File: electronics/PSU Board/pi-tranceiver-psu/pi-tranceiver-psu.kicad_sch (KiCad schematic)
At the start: 37 parts, among them IC1 LTC4368IMS-2#PBF, Q1 DMT6002LPS-13, Q2 DMT6002LPS-13

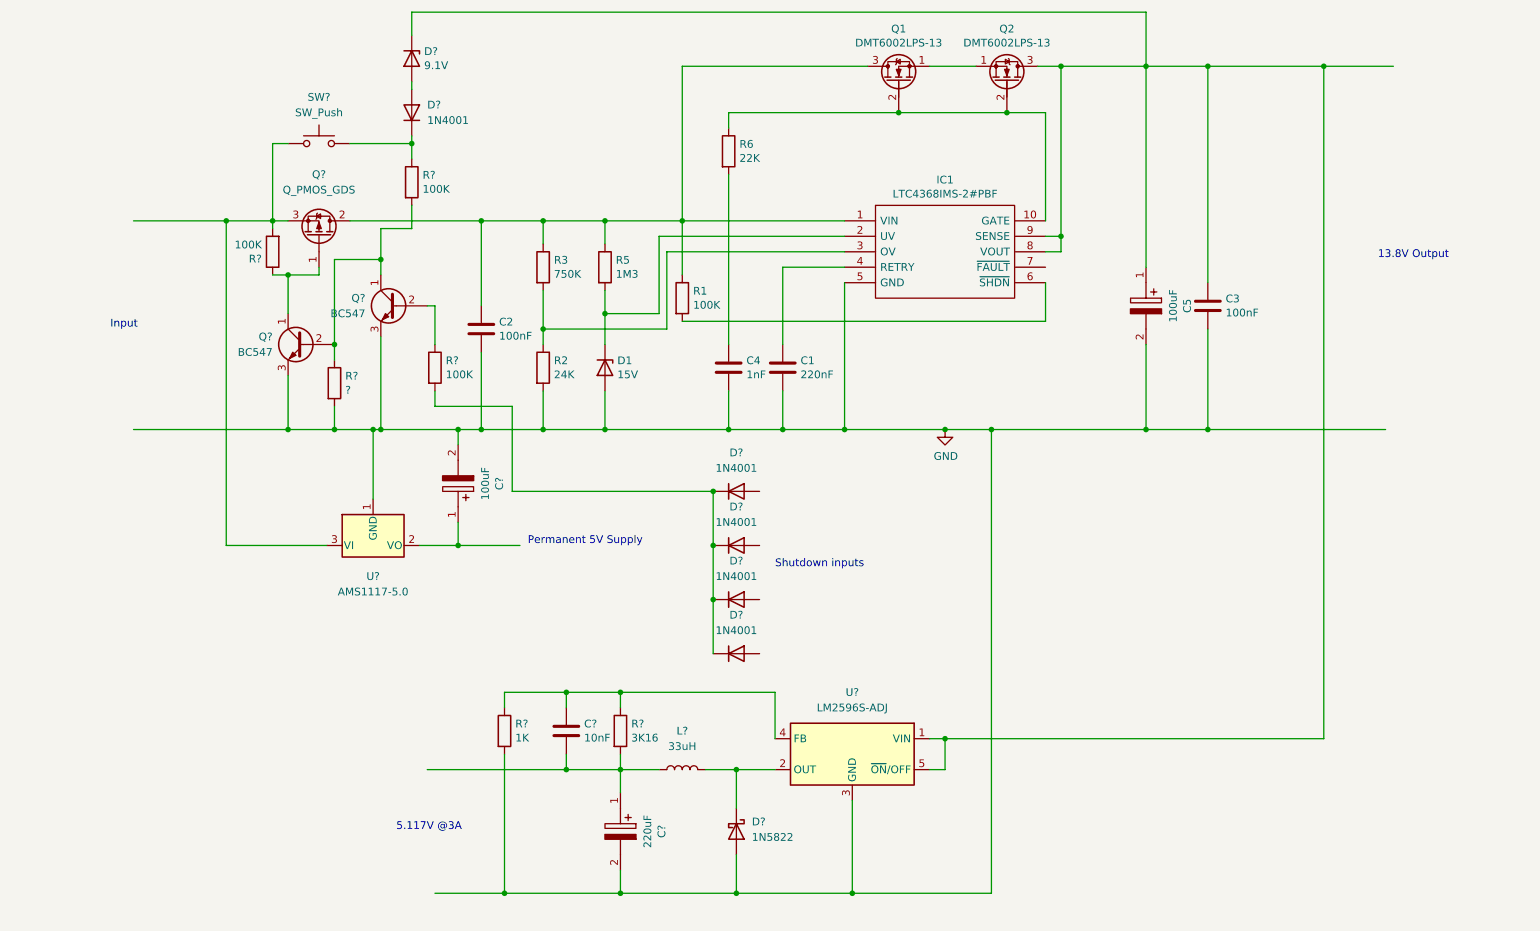
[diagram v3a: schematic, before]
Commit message: Added LM2679 details and project library
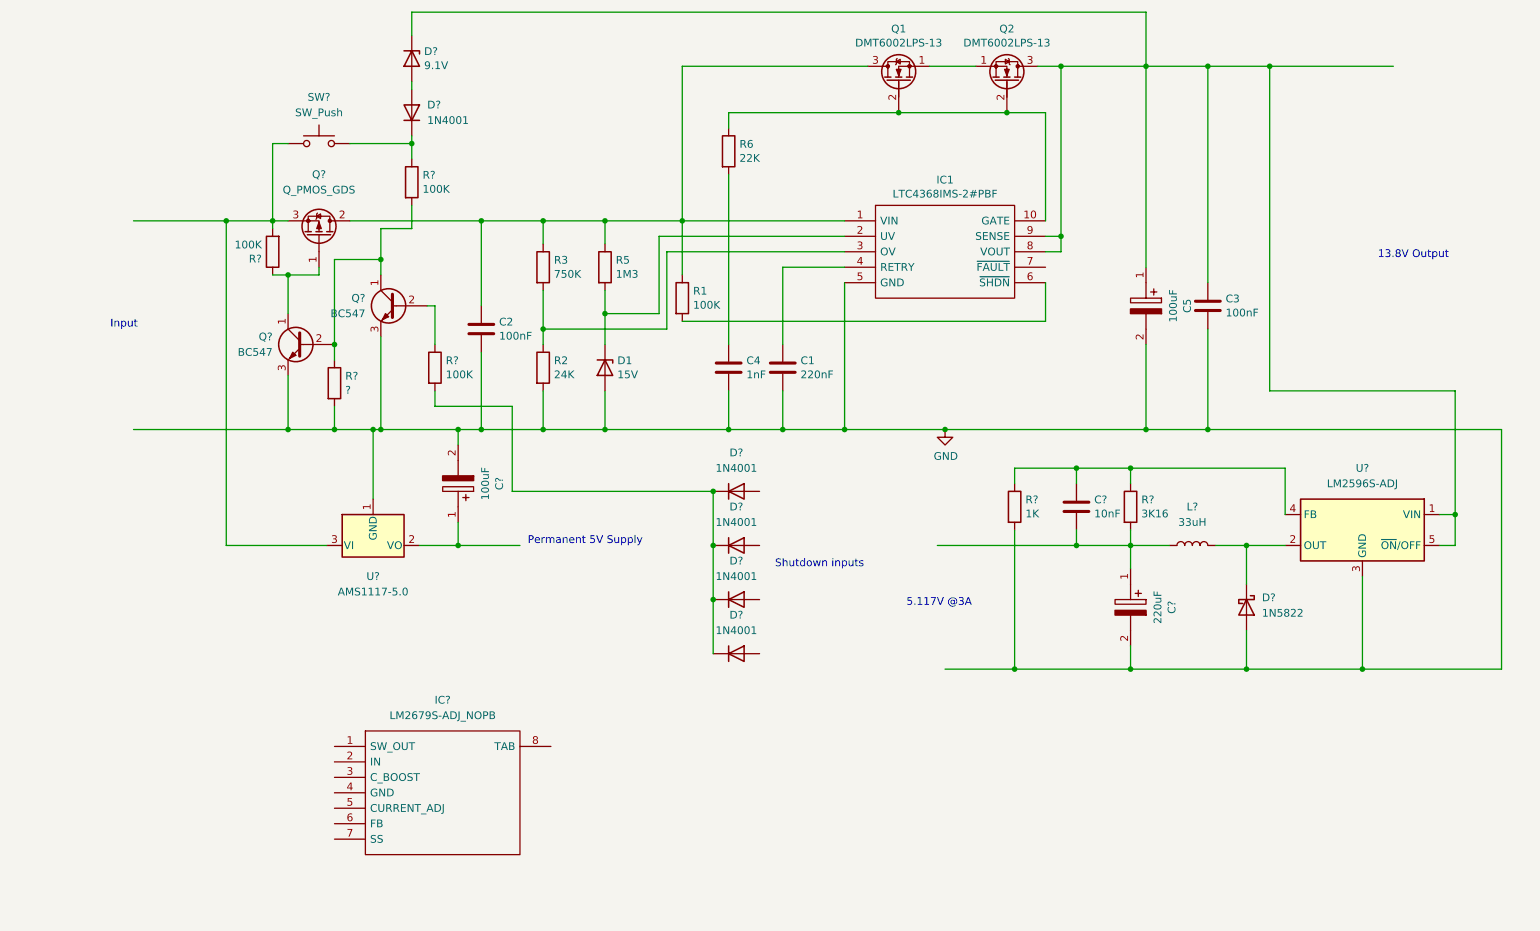
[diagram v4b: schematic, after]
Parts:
- added IC?: LM2679S-ADJ_NOPB, PSU_Board:TO127P1435X464-8N, symbol PSU_Board:LM2679S-ADJ_NOPB
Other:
- moved on the sheet: C?, D?, L?, R?, U?

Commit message: New PSU Design and added connectors
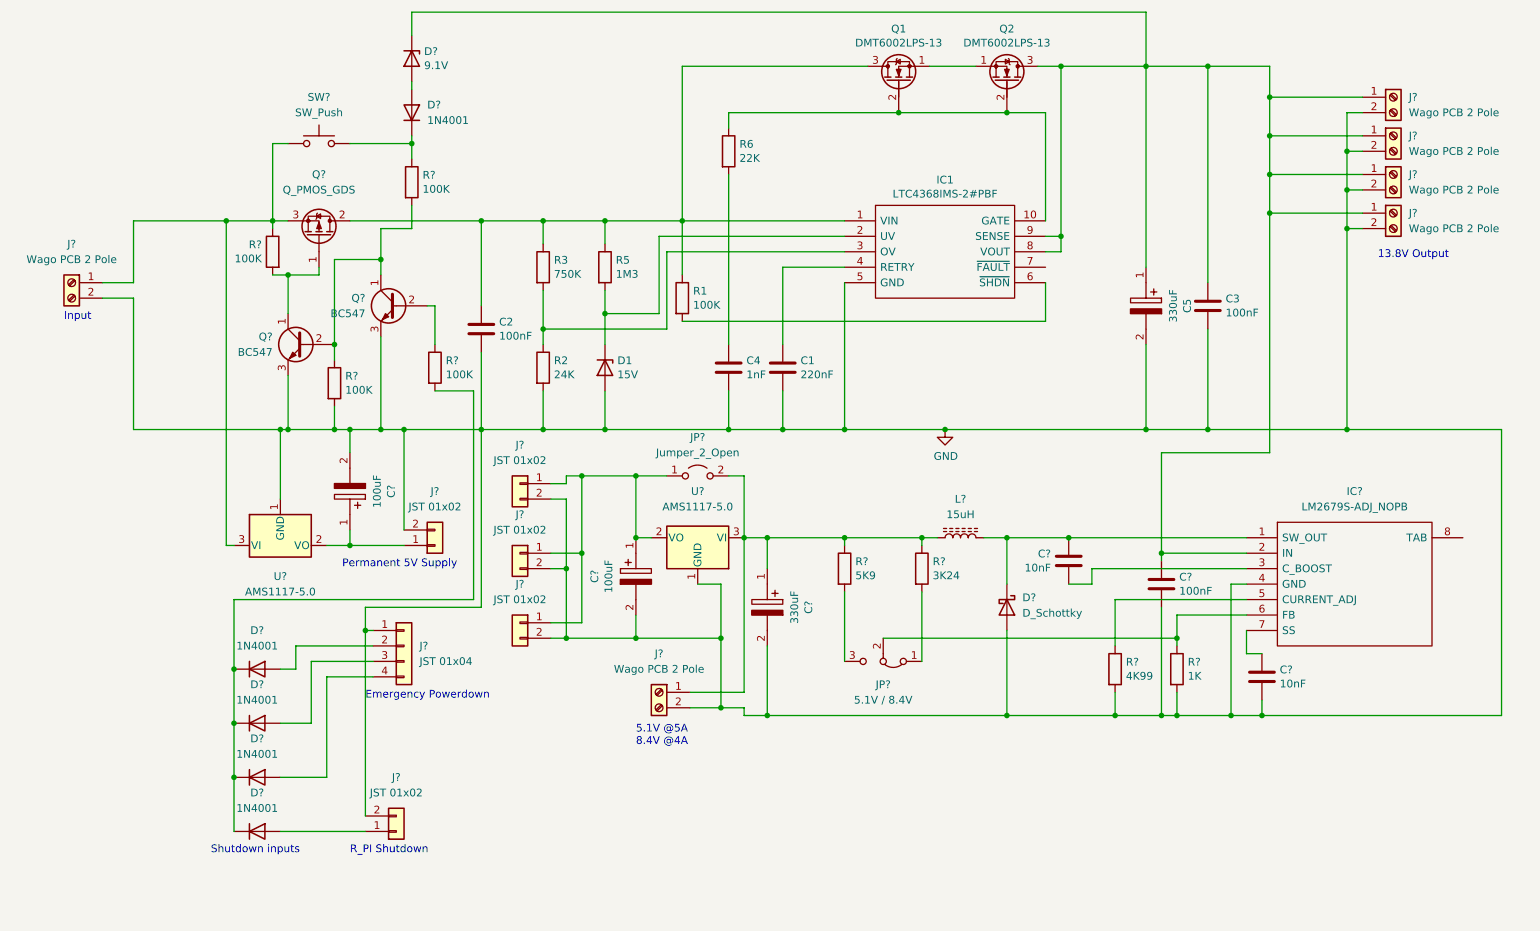
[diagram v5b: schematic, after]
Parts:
- removed C?: 10nF, Capacitor_SMD:C_0805_2012Metric_Pad1.18x1.45mm_HandSolder, symbol Device:C
- removed C?: 220uF, CAPAE660X770N, symbol SamacSys_Parts:865080545012
- removed D?: 1N5822, symbol Device:D_Schottky
- removed L?: 33uH, symbol Device:L
- removed R?: 3K16, Resistor_SMD:R_0805_2012Metric_Pad1.20x1.40mm_HandSolder, symbol Device:R
- removed R?: 1K, Resistor_SMD:R_0805_2012Metric_Pad1.20x1.40mm_HandSolder, symbol Device:R
- removed U?: LM2596S-ADJ, Package_TO_SOT_SMD:TO-263-5_TabPin3, symbol Regulator_Switching:LM2596S-ADJ
- added C?: 330uF, CAPAE660X770N, symbol SamacSys_Parts:865080545012
- added C? (x2): 10nF, Capacitor_SMD:C_1206_3216Metric_Pad1.33x1.80mm_HandSolder, symbol Device:C
- added C?: 100uF, CAPAE660X770N, symbol SamacSys_Parts:865080545012
- added C?: 100nF, Capacitor_SMD:C_1206_3216Metric_Pad1.33x1.80mm_HandSolder, symbol Device:C
- added D?: D_Schottky, symbol Device:D_Schottky
- added J? (x5): JST 01x02, symbol Connector_Generic:Conn_01x02
- added J? (x6): Wago PCB 2 Pole, symbol Connector:Screw_Terminal_01x02
- added J?: JST 01x04, symbol Connector_Generic:Conn_01x04
- added JP?: 5.1V / 8.4V, symbol Jumper:Jumper_3_Bridged12
- added JP?: Jumper_2_Open, symbol Jumper:Jumper_2_Open
- added L?: 15uH, symbol Device:L_Ferrite
- added R?: 4K99, Resistor_SMD:R_0805_2012Metric_Pad1.20x1.40mm_HandSolder, symbol Device:R
- added R?: 5K9, Resistor_SMD:R_0805_2012Metric_Pad1.20x1.40mm_HandSolder, symbol Device:R
- added R?: 1K, Resistor_SMD:R_0805_2012Metric_Pad1.20x1.40mm_HandSolder, symbol Device:R
- added R?: 3K24, Resistor_SMD:R_0805_2012Metric_Pad1.20x1.40mm_HandSolder, symbol Device:R
- added U?: AMS1117-5.0, Package_TO_SOT_SMD:SOT-223-3_TabPin2, symbol Regulator_Linear:AMS1117-5.0
- C5: value 100uF -> 330uF
- R?: value ? -> 100K
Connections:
- net GND: now also IC?.4 (GND), C?.2, C?.2, C?.2, C?.2, D?.2 (A), J?.1 (Pin_1), J?.2 (Pin_2), J?.2 (Pin_2), J?.2 (Pin_2), J?.2 (Pin_2), J?.2 (Pin_2), J?.2 (Pin_2), J?.2 (Pin_2), J?.2 (Pin_2), J?.2 (Pin_2), J?.2 (Pin_2), J?.2 (Pin_2), R?.2, R?.2, U?.1 (GND)
- net at C3.1, C5.1, D?.1 (K)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: now also IC?.2 (IN), C?.1, J?.1 (Pin_1), J?.1 (Pin_1), J?.1 (Pin_1), J?.1 (Pin_1)
- net at D?.2 (A): now also J?.4 (Pin_4)
- net at Q?.1 (C), Q?.1 (G): now also R?.2; no longer R?.1
- net at Q?.3 (S), SW?.1, U?.3 (VI): now also R?.1, J?.1 (Pin_1); no longer R?.2
- net at D?.2 (A): now also J?.3 (Pin_3)
- net at IC?.1 (SW_OUT): now also C?.1, D?.1 (K), L?.2
- net at IC?.3 (C_BOOST): now also C?.2
- net at IC?.5 (CURRENT_ADJ): now also R?.1
- net at IC?.6 (FB): now also JP?.2 (C), R?.1
- net at IC?.7 (SS): now also C?.1
- net at D?.2 (A): now also J?.2 (Pin_2)
- net at C?.1, U?.2 (VO): now also J?.1 (Pin_1)
- net at D?.2 (A): now also J?.1 (Pin_1)
- new net: C?.1, J?.1 (Pin_1), J?.1 (Pin_1), J?.1 (Pin_1), JP?.1 (A), U?.2 (VO)
- new net: C?.1, J?.1 (Pin_1), JP?.2 (B), L?.1, R?.1, R?.1, U?.3 (VI)
- new net: JP?.1 (A), R?.2
- new net: JP?.3 (B), R?.2
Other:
- note added: "5.1V @5A 8.4V @4A"
- note added: "Emergency Powerdown"
- note added: "R_PI Shutdown"
- note removed: "5.117V @3A"
- moved on the sheet: C?, D?, IC?, R?, U?

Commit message: All of the changes on Gareth's branch vs current main (#44)
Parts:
- added D10: 1N4001, Diode_THT:D_DO-41_SOD81_P10.16mm_Horizontal, symbol Diode:1N4001
- added D5: 4.3V, Diode_SMD:D_0805_2012Metric, symbol Device:D_Zener
- added R10: 100K, Resistor_SMD:R_0805_2012Metric_Pad1.20x1.40mm_HandSolder, symbol Device:R
- C10, C11: renamed from C?; footprint CAPAE660X770N -> Capacitor_SMD:CP_Elec_6.3x4.5
- C5: footprint CAPAE660X770N -> Capacitor_SMD:CP_Elec_6.3x4.5
- C9: renamed from C?; footprint CAPAE660X770N -> Capacitor_SMD:CP_Elec_16x22
- IC1: footprint SOP50P490X110-10N -> PSU_Board:SOP50P490X110-10N
- J1, J2, J3, J4, J5, J6: renamed from J?; value Wago PCB 2 Pole -> Phoenix PT2,5; footprint (none) -> TerminalBlock_Phoenix:TerminalBlock_Phoenix_PT-1,5-2-5.0-H_1x02_P5.00mm_Horizontal
- L1: renamed from L?; footprint (none) -> PSU_Board:SRP1265C-150M
- Q1, Q2: footprint SamacSys_Parts:PowerDI5060-8 -> PSU_Board:DMT6002LPS13
- R4: renamed from R?; value 100K -> 10K
- gave numbers to parts that had none: 32
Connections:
- net GND: now also R10.2
- net at C10.1, J7.1 (Pin_1), J8.1 (Pin_1)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: now also D5.1 (K)
- net at D6.1 (K), D7.1 (K), D8.1 (K)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: now also D10.1 (K), R10.1
- new net: D10.2 (A), D5.2 (A)
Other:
- moved on the sheet: R9

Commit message: Update pi-tranceiver-psu.kicad_sch
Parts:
- removed J10: JST 01x02, symbol Connector_Generic:Conn_01x02
- added D11: 9.1V, Diode_SMD:D_0805_2012Metric, symbol Device:D_Zener
- added J10: JST 01x04, symbol Connector_Generic:Conn_01x04
- added J13: JST 01x02, symbol Connector_Generic:Conn_01x02
- added J14: Phoenix PT2,5, TerminalBlock_Phoenix:TerminalBlock_Phoenix_PT-1,5-2-5.0-H_1x02_P5.00mm_Horizontal, symbol Connector:Screw_Terminal_01x02
- added Q6: BC547, Package_TO_SOT_THT:TO-92_Inline, symbol Transistor_BJT:BC547
- added R15, R17: 100K, Resistor_SMD:R_0805_2012Metric_Pad1.20x1.40mm_HandSolder, symbol Device:R
- added R16: 10K, Resistor_SMD:R_0805_2012Metric_Pad1.20x1.40mm_HandSolder, symbol Device:R
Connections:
- net GND: now also J10.1 (Pin_1), J13.1 (Pin_1), Q6.3 (E), R17.1
- net at C3.1, C5.1, D2.1 (K)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: now also J14.1 (Pin_1); no longer C7.1, IC2.2 (IN)
- net at C10.1, D5.1 (K), J7.1 (Pin_1)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: now also R15.1
- net at D9.2 (A): now also J10.2 (Pin_2)
- new net: J10.4 (Pin_4), J13.2 (Pin_2)
- new net: J10.3 (Pin_3), Q6.1 (C), R15.2
- new net: C7.1, D11.1 (K), IC2.2 (IN), J14.2 (Pin_2)
- new net: Q6.2 (B), R16.2, R17.2
- new net: D11.2 (A), R16.1
